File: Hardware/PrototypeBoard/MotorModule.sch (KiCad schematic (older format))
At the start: 14 parts

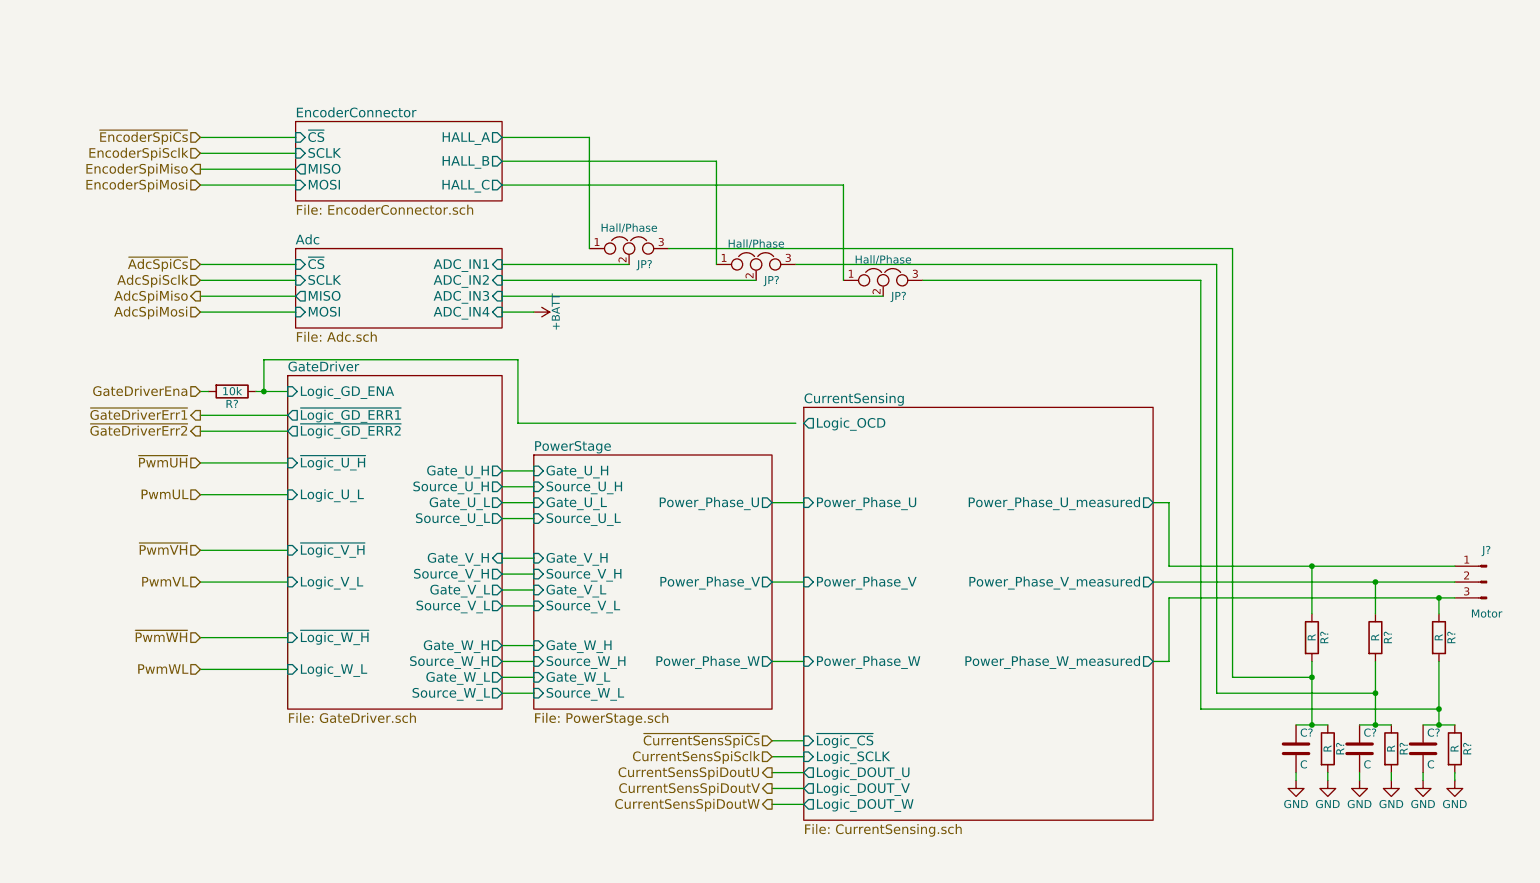
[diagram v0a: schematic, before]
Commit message: Fixed all ERC errors. Added power consumption estimation and other comments. Added links to datasheets. Dimensioned low pass and voltage dividers. Added TVS diodes for protection of voltage rails and ADC inputs. Added fuses. Added Testpoints. Added DC-link capacitors.
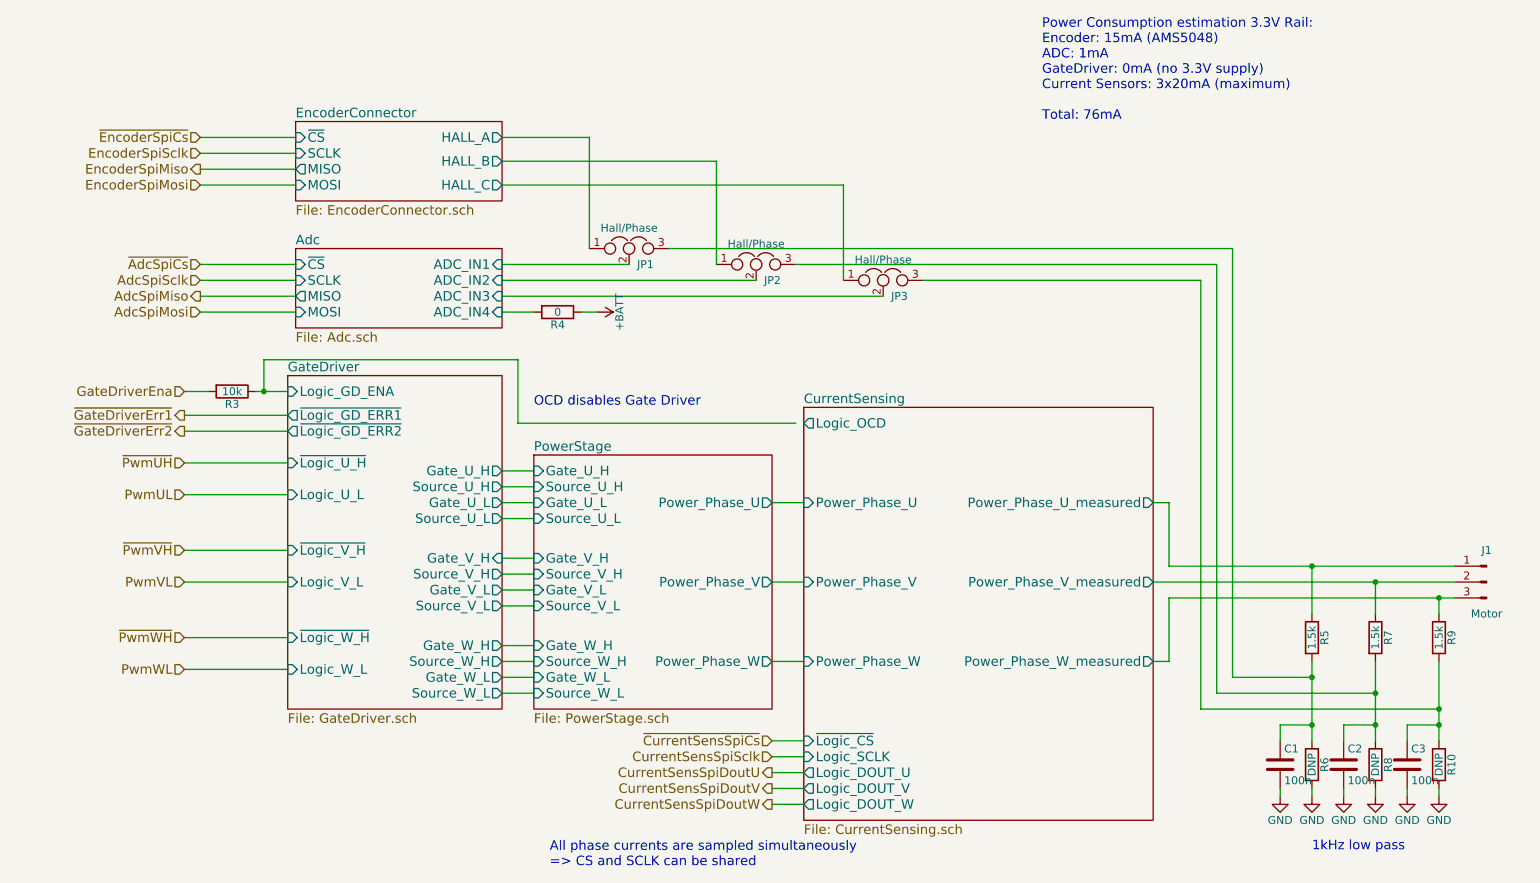
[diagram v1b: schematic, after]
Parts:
- added R4: 0, symbol R
- C1, C2, C3: renamed from C?; value C -> 100n
- R10, R6, R8: renamed from R?; value R -> DNP
- R5, R7, R9: renamed from R?; value R -> 1.5k
- gave numbers to parts that had none: 5
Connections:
- net +BATT: now also R4.1
- new net Adc/ADC_IN4: R4.2
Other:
- note added: "1kHz low pass"
- note added: "All phase currents are sampled simultaneously\n=> CS and SCLK can be shared"
- note added: "OCD disables Gate Driver"
- note added: "Power Consumption estimation 3.3V Rail:\nEncoder: 15mA (AMS5048)\nADC: 1mA\nGateDriver: 0mA (no 3.3V supply)\nCurrent Sensors: 3x20mA (maximum)\n\nTotal: 76mA"
- moved on the sheet: C1, C2, C3, R10, R6, R8

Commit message: forgot files
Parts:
- C1, C2, C3: footprint (none) -> Capacitors_SMD:C_0805_HandSoldering
- J1: footprint (none) -> Pin_Headers:Pin_Header_Angled_1x03_Pitch2.54mm
- JP1, JP2, JP3: footprint (none) -> Connectors:PINHEAD1-3
- R10, R3, R4, R5, R6, R7, R8, R9: footprint (none) -> Resistors_SMD:R_0805_HandSoldering
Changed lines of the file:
@@
 F 0 "R3" V 2980 3200 50  0000 C CNN
 F 1 "10k" V 2900 3200 50  0000 C CNN
-F 2 "" V 2830 3200 50  0001 C CNN
+F 2 "Resistors_SMD:R_0805_HandSoldering" V 2830 3200 50  0001 C CNN
 F 3 "" H 2900 3200 50  0001 C CNN
 	1    2900 3200
@@
 F 0 "J1" H 10800 4600 50  0000 C CNN
 F 1 "Motor" H 10800 4200 50  0000 C CNN
-F 2 "" H 10800 4400 50  0001 C CNN
+F 2 "Pin_Headers:Pin_Header_Angled_1x03_Pitch2.54mm" H 10800 4400 50  0001 C CNN
 F 3 "" H 10800 4400 50  0001 C CNN
 	1    10800 4400
@@
 F 0 "R5" V 9780 4750 50  0000 C CNN
 F 1 "1.5k" V 9700 4750 50  0000 C CNN
-F 2 "" V 9630 4750 50  0001 C CNN
+F 2 "Resistors_SMD:R_0805_HandSoldering" V 9630 4750 50  0001 C CNN
 F 3 "" H 9700 4750 50  0001 C CNN
 	1    9700 4750
@@
 F 0 "R7" V 10180 4750 50  0000 C CNN
 F 1 "1.5k" V 10100 4750 50  0000 C CNN
-F 2 "" V 10030 4750 50  0001 C CNN
+F 2 "Resistors_SMD:R_0805_HandSoldering" V 10030 4750 50  0001 C CNN
 F 3 "" H 10100 4750 50  0001 C CNN
 	1    10100 4750
@@
 F 0 "R9" V 10580 4750 50  0000 C CNN
 F 1 "1.5k" V 10500 4750 50  0000 C CNN
-F 2 "" V 10430 4750 50  0001 C CNN
+F 2 "Resistors_SMD:R_0805_HandSoldering" V 10430 4750 50  0001 C CNN
 F 3 "" H 10500 4750 50  0001 C CNN
 	1    10500 4750
@@
 F 0 "C1" H 9525 5650 50  0000 L CNN
 F 1 "100n" H 9525 5450 50  0000 L CNN
-F 2 "" H 9538 5400 50  0001 C CNN
+F 2 "Capacitors_SMD:C_0805_HandSoldering" H 9538 5400 50  0001 C CNN
 F 3 "" H 9500 5550 50  0001 C CNN
 	1    9500 5550
@@
 F 0 "C2" H 9925 5650 50  0000 L CNN
 F 1 "100n" H 9925 5450 50  0000 L CNN
-F 2 "" H 9938 5400 50  0001 C CNN
+F 2 "Capacitors_SMD:C_0805_HandSoldering" H 9938 5400 50  0001 C CNN
 F 3 "" H 9900 5550 50  0001 C CNN
 	1    9900 5550
@@
 F 0 "C3" H 10325 5650 50  0000 L CNN
 F 1 "100n" H 10325 5450 50  0000 L CNN
-F 2 "" H 10338 5400 50  0001 C CNN
+F 2 "Capacitors_SMD:C_0805_HandSoldering" H 10338 5400 50  0001 C CNN
 F 3 "" H 10300 5550 50  0001 C CNN
 	1    10300 5550
@@
 F 0 "R6" V 9780 5550 50  0000 C CNN
 F 1 "DNP" V 9700 5550 50  0000 C CNN
-F 2 "" V 9630 5550 50  0001 C CNN
+F 2 "Resistors_SMD:R_0805_HandSoldering" V 9630 5550 50  0001 C CNN
 F 3 "" H 9700 5550 50  0001 C CNN
 	1    9700 5550
@@
 F 0 "R8" V 10180 5550 50  0000 C CNN
 F 1 "DNP" V 10100 5550 50  0000 C CNN
-F 2 "" V 10030 5550 50  0001 C CNN
+F 2 "Resistors_SMD:R_0805_HandSoldering" V 10030 5550 50  0001 C CNN
 F 3 "" H 10100 5550 50  0001 C CNN
 	1    10100 5550
@@
 F 0 "R10" V 10580 5550 50  0000 C CNN
 F 1 "DNP" V 10500 5550 50  0000 C CNN
-F 2 "" V 10430 5550 50  0001 C CNN
+F 2 "Resistors_SMD:R_0805_HandSoldering" V 10430 5550 50  0001 C CNN
 F 3 "" H 10500 5550 50  0001 C CNN
 	1    10500 5550
@@
 F 0 "JP1" H 5450 2200 50  0000 L CNN
 F 1 "Hall/Phase" H 5400 2400 50  0000 C BNN
-F 2 "" H 5400 2300 50  0001 C CNN
+F 2 "Connectors:PINHEAD1-3" H 5400 2300 50  0001 C CNN
 F 3 "" H 5400 2300 50  0001 C CNN
 	1    5400 2300
@@
 F 0 "JP2" H 6250 2300 50  0000 L CNN
 F 1 "Hall/Phase" H 6200 2500 50  0000 C BNN
-F 2 "" H 6200 2400 50  0001 C CNN
+F 2 "Connectors:PINHEAD1-3" H 6200 2400 50  0001 C CNN
 F 3 "" H 6200 2400 50  0001 C CNN
 	1    6200 2400
@@
 F 0 "JP3" H 7050 2400 50  0000 L CNN
 F 1 "Hall/Phase" H 7000 2600 50  0000 C BNN
-F 2 "" H 7000 2500 50  0001 C CNN
+F 2 "Connectors:PINHEAD1-3" H 7000 2500 50  0001 C CNN
 F 3 "" H 7000 2500 50  0001 C CNN
 	1    7000 2500
@@
 F 0 "R4" V 5030 2700 50  0000 C CNN
 F 1 "0" V 4950 2700 50  0000 C CNN
-F 2 "" V 4880 2700 50  0001 C CNN
+F 2 "Resistors_SMD:R_0805_HandSoldering" V 4880 2700 50  0001 C CNN
 F 3 "" H 4950 2700 50  0001 C CNN
 	1    4950 2700

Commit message: assigned net classes and a few net names
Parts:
- JP1, JP2, JP3: footprint Connectors:PINHEAD1-3 -> Connectors:GS3
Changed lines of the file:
@@
 F 0 "JP1" H 5450 2200 50  0000 L CNN
 F 1 "Hall/Phase" H 5400 2400 50  0000 C BNN
-F 2 "Connectors:PINHEAD1-3" H 5400 2300 50  0001 C CNN
+F 2 "Connectors:GS3" H 5400 2300 50  0001 C CNN
 F 3 "" H 5400 2300 50  0001 C CNN
 	1    5400 2300
@@
 F 0 "JP2" H 6250 2300 50  0000 L CNN
 F 1 "Hall/Phase" H 6200 2500 50  0000 C BNN
-F 2 "Connectors:PINHEAD1-3" H 6200 2400 50  0001 C CNN
+F 2 "Connectors:GS3" H 6200 2400 50  0001 C CNN
 F 3 "" H 6200 2400 50  0001 C CNN
 	1    6200 2400
@@
 F 0 "JP3" H 7050 2400 50  0000 L CNN
 F 1 "Hall/Phase" H 7000 2600 50  0000 C BNN
-F 2 "Connectors:PINHEAD1-3" H 7000 2500 50  0001 C CNN
+F 2 "Connectors:GS3" H 7000 2500 50  0001 C CNN
 F 3 "" H 7000 2500 50  0001 C CNN
 	1    7000 2500

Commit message: more layout and some changes to schematic
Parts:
- removed J1: Motor, Pin_Headers:Pin_Header_Angled_1x03_Pitch2.54mm, symbol Conn_01x03_Male
- added J1: Conn_01x03, Connectors_Phoenix:PhoenixContact_MSTBA-G_03x5.08mm_Angled, symbol Conn_01x03
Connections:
- net GateDriver/Logic_GD_ENA is gone; now on net CurrentSensing/Logic_OCD: R3.1
- net CurrentSensing/Power_Phase_U_measured: now also J1.3 (Pin_3)
- net CurrentSensing/Power_Phase_V_measured: now also J1.2 (Pin_2)
- net CurrentSensing/Power_Phase_W_measured: now also J1.1 (Pin_1)
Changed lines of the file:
@@
 $EndSheet
-$Comp
-L Conn_01x03_Male J1
-U 1 1 5AFEE147
-P 10800 4400
-F 0 "J1" H 10800 4600 50  0000 C CNN
-F 1 "Motor" H 10800 4200 50  0000 C CNN
-F 2 "Pin_Headers:Pin_Header_Angled_1x03_Pitch2.54mm" H 10800 4400 50  0001 C CNN
-F 3 "" H 10800 4400 50  0001 C CNN
-	1    10800 4400
-	-1   0    0    -1
-$EndComp
 $Comp
 L R R5
@@
 	4600 5100 4800 5100
 Wire Wire Line
-	6450 3400 4700 3400
+	4700 3400 6500 3400
 Wire Wire Line
 	3050 3200 3250 3200
@@
 Connection ~ 10100 5300
 Connection ~ 10500 5300
+$Comp
+L Conn_01x03 J1
+U 1 1 5B23EBC2
+P 10800 4400
+F 0 "J1" H 10800 4600 50  0000 C CNN
+F 1 "Conn_01x03" H 10800 4200 50  0000 C CNN
+F 2 "Connectors_Phoenix:PhoenixContact_MSTBA-G_03x5.08mm_Angled" H 10800 4400 50  0001 C CNN
+F 3 "" H 10800 4400 50  0001 C CNN
+	1    10800 4400
+	1    0    0    1
+$EndComp
 $EndSCHEMATC

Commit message: Migrated to kicad 5
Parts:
- C1, C2, C3: symbol C -> Device:C
- J1: symbol Conn_01x03 -> conn:Conn_01x03
- JP1, JP2, JP3: symbol Jumper_NC_Dual -> Device:Jumper_NC_Dual
- R10, R3, R4, R5, R6, R7, R8, R9: symbol R -> Device:R
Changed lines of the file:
@@
-EESchema Schematic File Version 2
-LIBS:power
-LIBS:device
-LIBS:switches
-LIBS:relays
-LIBS:motors
-LIBS:transistors
-LIBS:conn
-LIBS:linear
-LIBS:regul
-LIBS:74xx
-LIBS:cmos4000
-LIBS:adc-dac
-LIBS:memory
-LIBS:xilinx
-LIBS:microcontrollers
-LIBS:dsp
-LIBS:microchip
-LIBS:analog_switches
-LIBS:motorola
-LIBS:texas
-LIBS:intel
-LIBS:audio
-LIBS:interface
-LIBS:digital-audio
-LIBS:philips
-LIBS:display
-LIBS:cypress
-LIBS:siliconi
-LIBS:opto
-LIBS:atmel
-LIBS:contrib
-LIBS:valves
+EESchema Schematic File Version 4
 LIBS:PrototypeBoard-cache
-EELAYER 25 0
+EELAYER 26 0
 EELAYER END
 $Descr A4 11693 8268
@@
 CurrentSensSpiSclk
 $Comp
-L R R3
+L Device:R R3
 U 1 1 5AFDCF78
 P 2900 3200
@@
 $EndSheet
 $Comp
-L R R5
+L Device:R R5
 U 1 1 5AFEF95E
 P 9700 4750
@@
 $EndComp
 $Comp
-L R R7
+L Device:R R7
 U 1 1 5AFEFDB0
 P 10100 4750
@@
 $EndComp
 $Comp
-L R R9
+L Device:R R9
 U 1 1 5AFEFF1D
 P 10500 4750
@@
 $EndComp
 $Comp
-L C C1
+L Device:C C1
 U 1 1 5AFF0BC1
 P 9500 5550
@@
 $EndComp
 $Comp
-L C C2
+L Device:C C2
 U 1 1 5AFF0D64
 P 9900 5550
@@
 $EndComp
 $Comp
-L C C3
+L Device:C C3
 U 1 1 5AFF0EA9
 P 10300 5550
@@
 $EndComp
 $Comp
-L GND #PWR05
+L power:GND #PWR05
 U 1 1 5AFF2590
 P 9500 5750
@@
 $EndComp
 $Comp
-L GND #PWR06
+L power:GND #PWR06
 U 1 1 5AFF26DA
 P 9900 5750
@@
 $EndComp
 $Comp
-L GND #PWR07
+L power:GND #PWR07
 U 1 1 5AFF281D
 P 10300 5750
@@
 $EndComp
 $Comp
-L R R6
+L Device:R R6
 U 1 1 5AFF3F78
 P 9700 5550
@@
 $EndComp
 $Comp
-L R R8
+L Device:R R8
 U 1 1 5AFF40FD
 P 10100 5550
@@
 $EndComp
 $Comp
-L R R10
+L Device:R R10
 U 1 1 5AFF424A
 P 10500 5550
@@
 $EndComp
 $Comp
-L GND #PWR08
+L power:GND #PWR08
 U 1 1 5AFF49CA
 P 9700 5750
@@
 $EndComp
 $Comp
-L GND #PWR09
+L power:GND #PWR09
 U 1 1 5AFF4BAF
 P 10100 5750
@@
 $EndComp
 $Comp
-L GND #PWR010
+L power:GND #PWR010
 U 1 1 5AFF4CF9
 P 10500 5750
@@
 $EndSheet
 $Comp
-L Jumper_NC_Dual JP1
+L Device:Jumper_NC_Dual JP1
 U 1 1 5AFFD01D
 P 5400 2300
@@
 $EndComp
 $Comp
-L Jumper_NC_Dual JP2
+L Device:Jumper_NC_Dual JP2
 U 1 1 5AFFD449
 P 6200 2400
@@
 $EndComp
 $Comp
-L Jumper_NC_Dual JP3
+L Device:Jumper_NC_Dual JP3
 U 1 1 5AFFD604
 P 7000 2500
@@
 $EndComp
 $Comp
-L +BATT #PWR011
+L power:+BATT #PWR011
 U 1 1 5AFFE539
 P 5200 2700
@@
 1kHz low pass
 $Comp
-L R R4
+L Device:R R4
 U 1 1 5B005AF3
 P 4950 2700
@@
 	4700 3400 6500 3400
 Wire Wire Line
-	3050 3200 3250 3200
+	3050 3200 3100 3200
 Wire Wire Line
 	4700 3400 4700 3000
@@
 	10300 5700 10300 5750
 Wire Wire Line
-	8700 4400 10600 4400
-Wire Wire Line
-	8800 4300 10600 4300
-Wire Wire Line
-	8800 4500 10600 4500
+	8700 4400 10100 4400
+Wire Wire Line
+	8800 4300 9700 4300
+Wire Wire Line
+	8800 4500 10500 4500
 Wire Wire Line
 	9700 5700 9700 5750
@@
 	5100 2700 5200 2700
 Wire Wire Line
-	9700 4900 9700 5400
-Wire Wire Line
-	10100 4900 10100 5400
-Wire Wire Line
-	10500 4900 10500 5400
+	9700 4900 9700 5000
+Wire Wire Line
+	10100 4900 10100 5100
+Wire Wire Line
+	10500 4900 10500 5200
 Wire Wire Line
 	9500 5400 9500 5300
@@
 Connection ~ 10500 5300
 $Comp
-L Conn_01x03 J1
+L conn:Conn_01x03 J1
 U 1 1 5B23EBC2
 P 10800 4400
@@
 	1    0    0    1
 $EndComp
+Wire Wire Line
+	3100 3200 3250 3200
+Wire Wire Line
+	9700 4300 10600 4300
+Wire Wire Line
+	10100 4400 10600 4400
+Wire Wire Line
+	10500 4500 10600 4500
+Wire Wire Line
+	10500 5200 10500 5300
+Wire Wire Line
+	10100 5100 10100 5300
+Wire Wire Line
+	9700 5000 9700 5300
+Wire Wire Line
+	9700 5300 9700 5400
+Wire Wire Line
+	10100 5300 10100 5400
+Wire Wire Line
+	10500 5300 10500 5400
 $EndSCHEMATC
